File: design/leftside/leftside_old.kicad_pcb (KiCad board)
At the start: 4 copper layers, 144 x 95.2 mm, 167 parts, among them IC2 XC9148G50CER-G, IC3 nRF52833-QDAA-R7, IC4 74AHCT125PW,118, IC5 MCP23018T-E_SS, IC6 XC9291B33D1R-G, J1 USB_C_Receptacle_USB2.0_16P, J2 Battery Pos, J3 Battery Neg, J4 OLED_128x32, J5 SFV12R-1STBE1HLF, J6 PinHeader_1x04_P2.54mm_Horizo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, U2 BQ24072RGT, U3 USB6B1, U4 BQ27441-G1, U5 PEC11L-4015F-S0015, U6 PEC11L-4015F-S0015, X1 32MHz

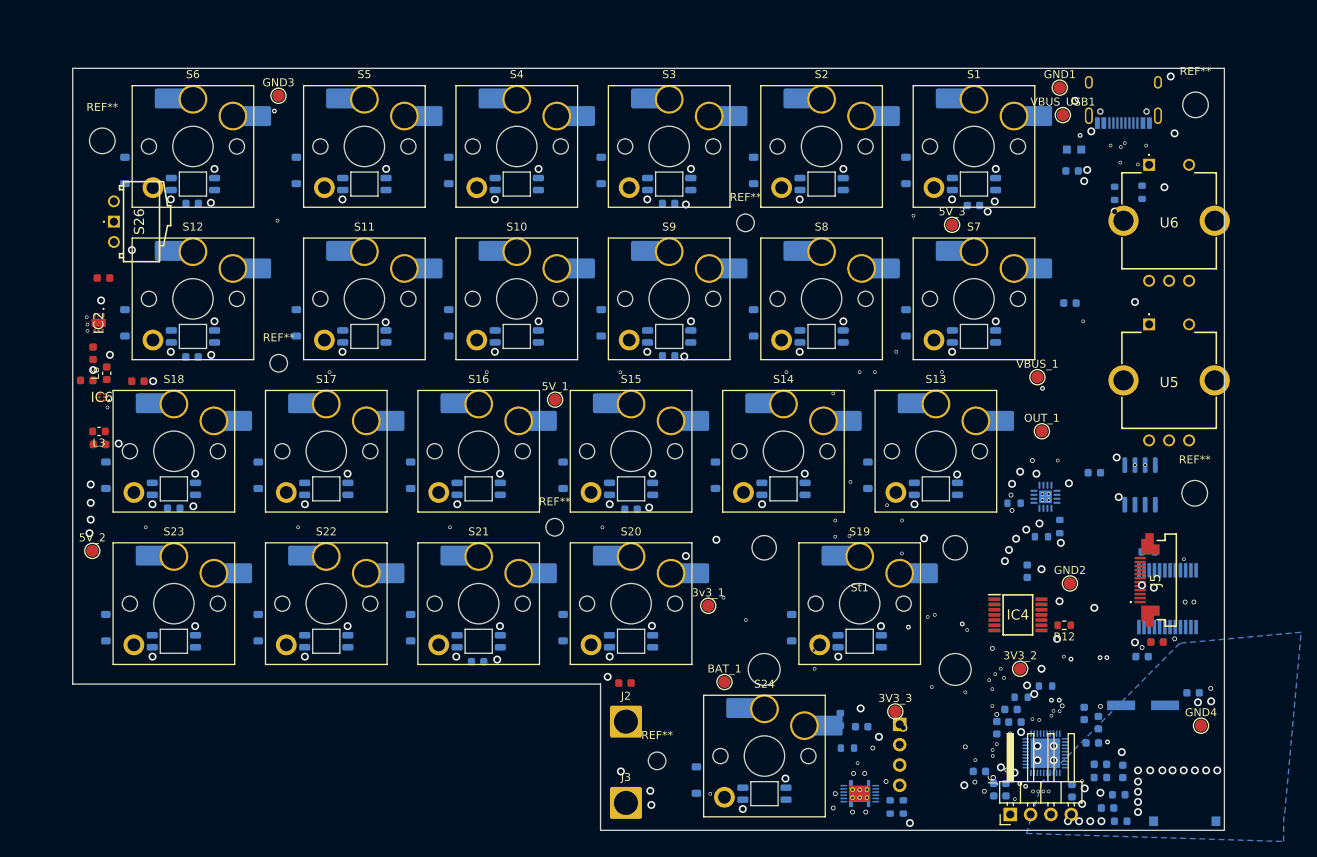
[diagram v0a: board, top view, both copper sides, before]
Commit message: successfully create pcb layout mirror script
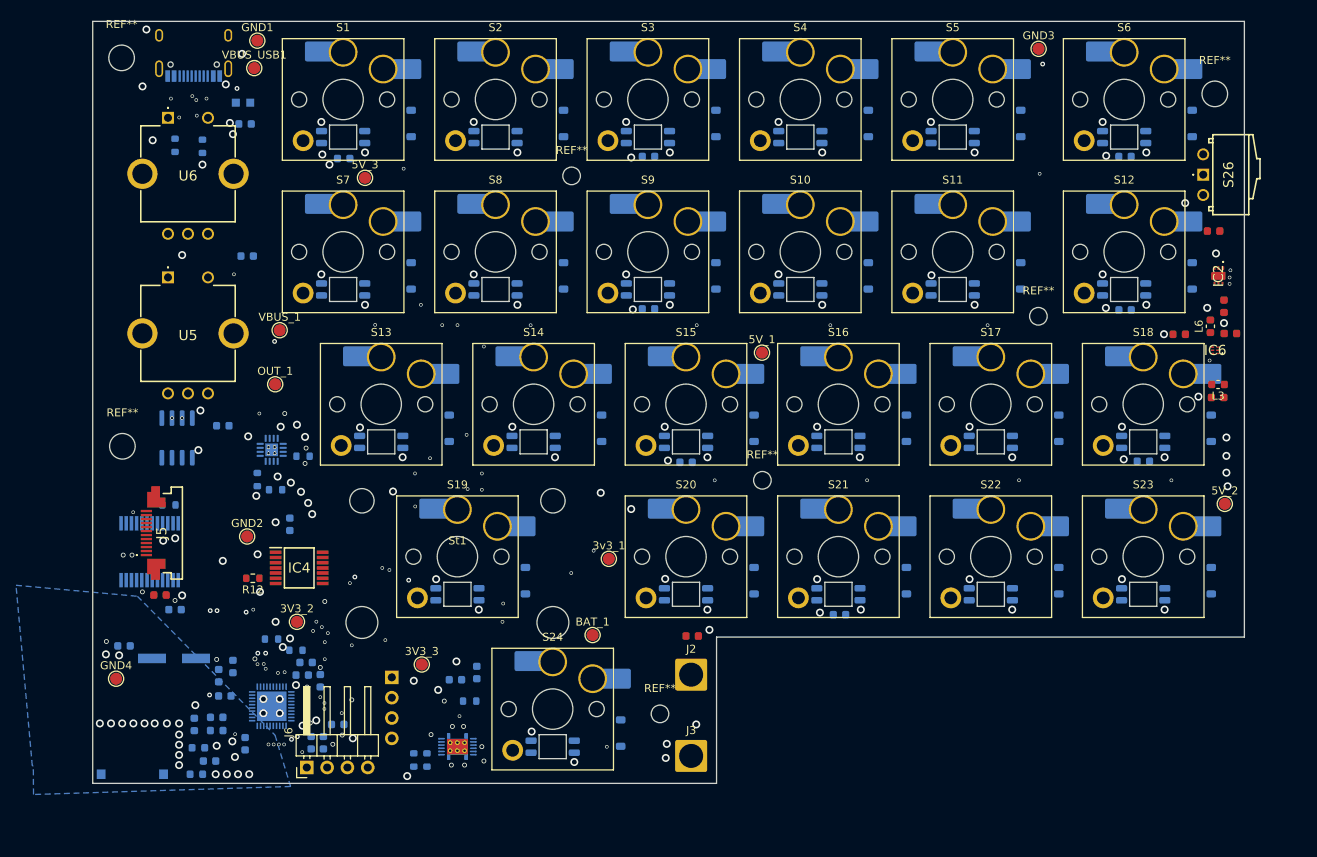
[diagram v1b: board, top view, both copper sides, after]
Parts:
- moved C27 143.1 mm to (201.4, 65.8)
- moved 5V_2 141.7 mm to (200.7, 87.1)
- moved C26 141.5 mm to (200.6, 62.4)
- moved IC2 140.1 mm to (199.9, 58.6)
- moved L3 140.0 mm to (199.9, 72.1)
- moved C13 139.9 mm to (199.8, 73.8)
- moved IC6 139.3 mm to (199.5, 67.9)
- moved REF** 139.2 mm to (199.5, 35.8)
- moved C25 138.9 mm to (199.3, 53.0)
- moved Di19 138.3 mm to (199.0, 77.6)
- moved Di23 138.3 mm to (199.0, 96.7)
- moved L6 138.1 mm to (198.9, 64.9)
- moved S26 136.3 mm to (198.0, 45.9)
- moved GND4 135.7 mm to (62.1, 108.9)
- moved REF** 134.4 mm to (62.8, 31.3)
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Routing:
- net unconnected-(U6-PadMH1): vias 1 -> 0
- net GND: vias 114 -> 115
- net 3V3: vias 12 -> 14
- net /VBUS: vias 4 -> 3
- net /SCL: vias 2 -> 1
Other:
- outline, holes or cut-outs redrawn
